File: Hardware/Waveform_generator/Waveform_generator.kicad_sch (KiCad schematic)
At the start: 101 parts, among them J1 Conn_01x02, J2 Conn_01x02, J3 Conn_01x02, J4 Conn_01x02, J5 PogoPin, J6 PogoPin, J7 GND_CHASIS, J8 GND_CHASIS, SW1 SW_DPDT_x2, U1 TPS54202DDC, U10 MCP4822, U11 LM1875, U2 TL072, U3 ESP32-DEVKITC-32U, U4 TSR1-2450E, U5 XC6206PxxxMR, U6 AD9837BCPZ-RL7, U7 TL072, U8 AD5160, U9 TL072, Y1 X1G0041710027

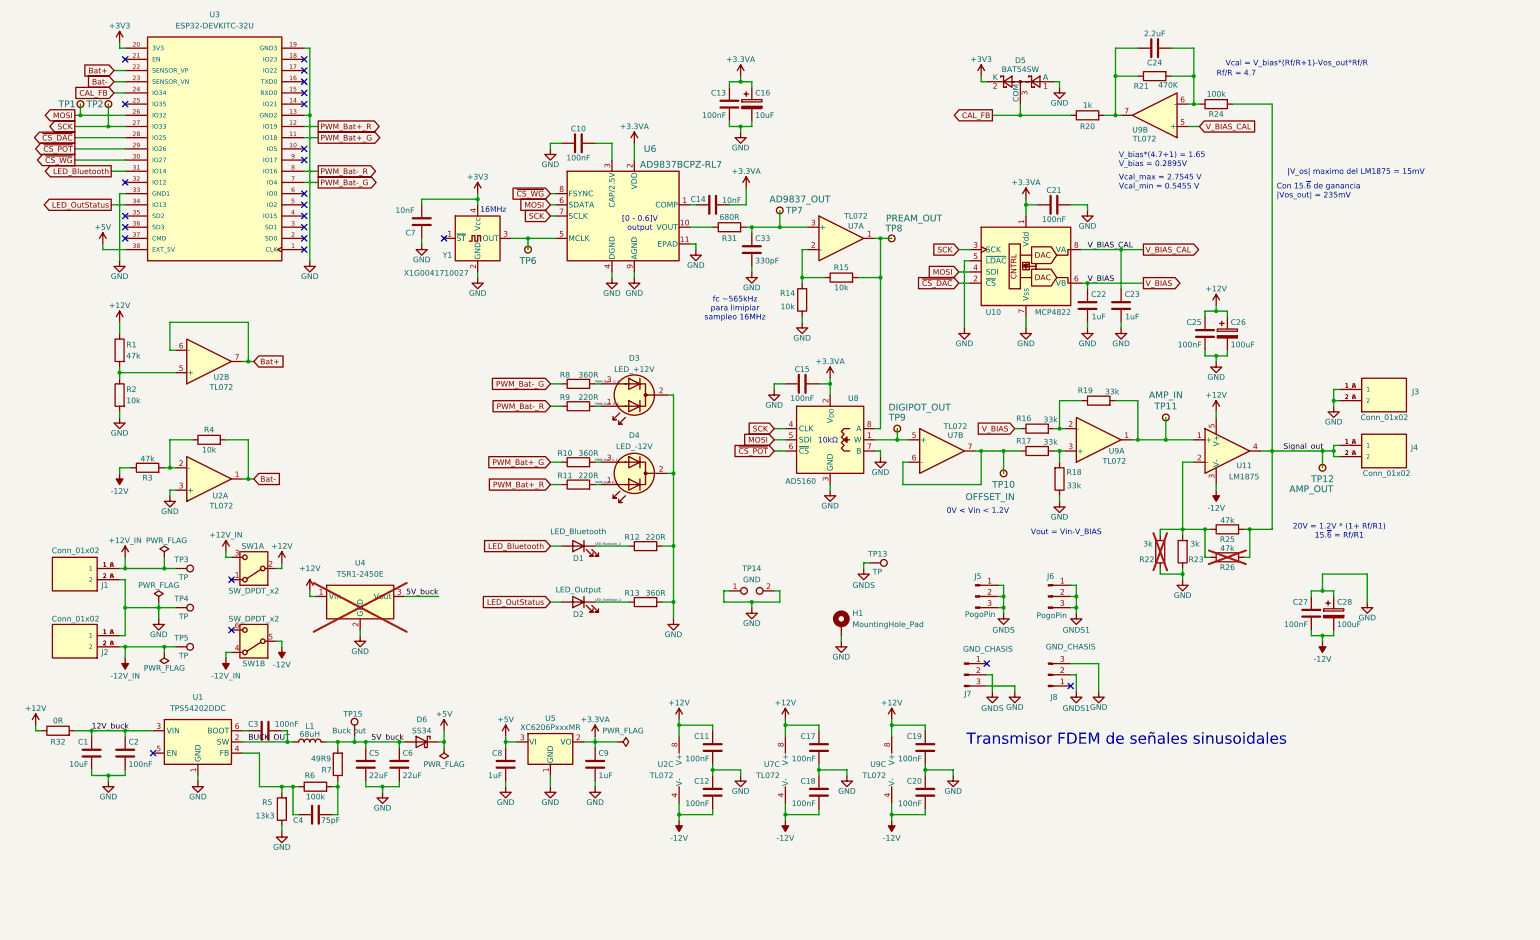
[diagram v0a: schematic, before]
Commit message: Añadido switch para el output en el esquemático
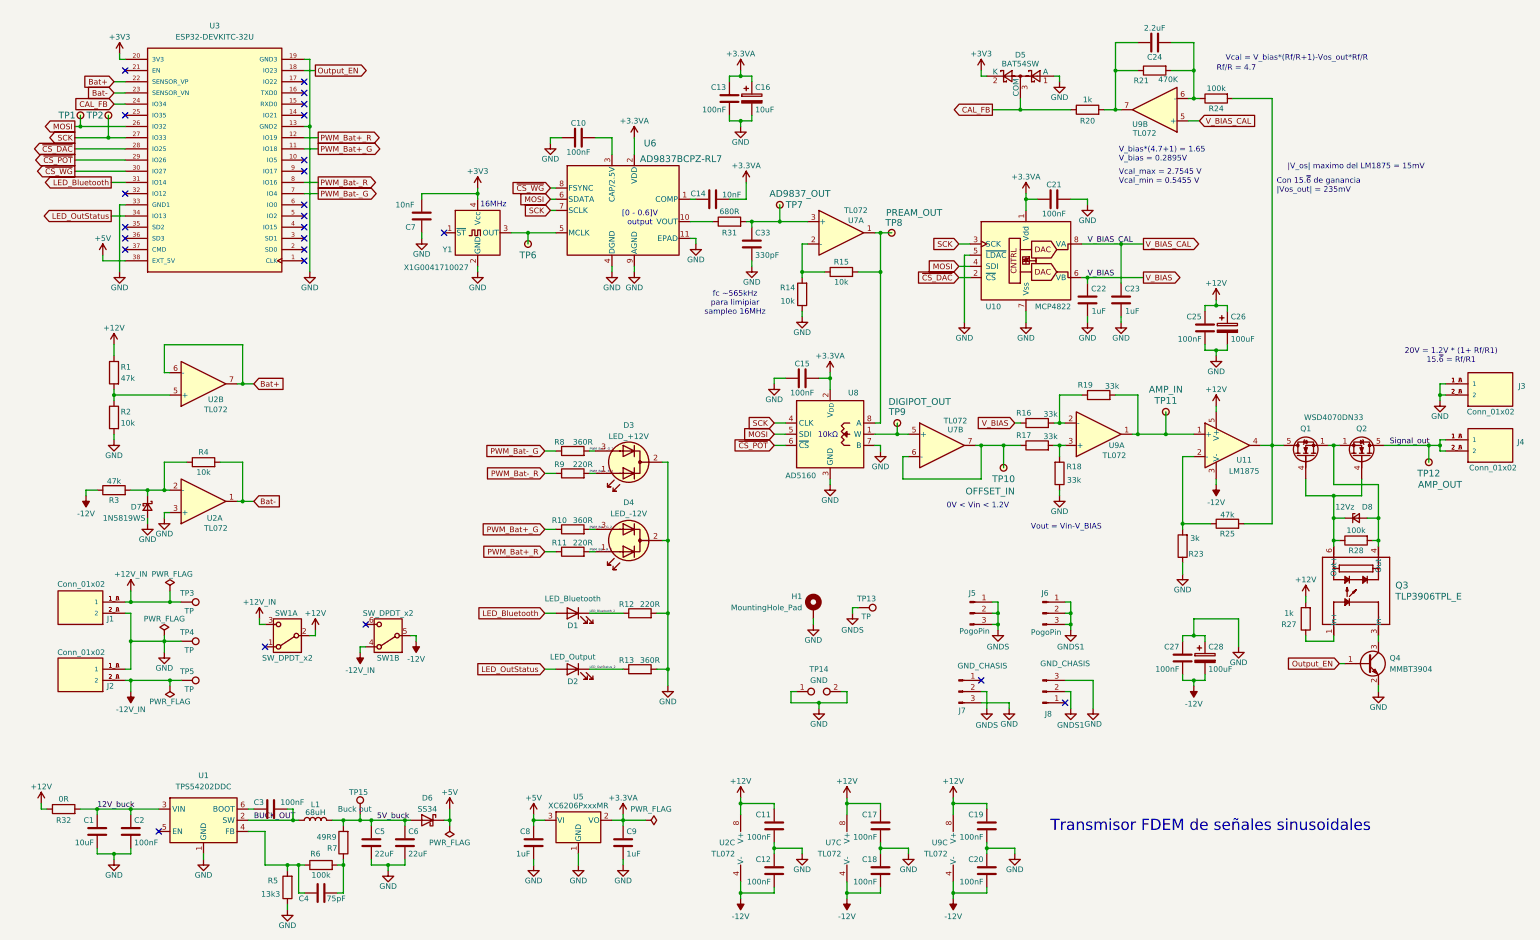
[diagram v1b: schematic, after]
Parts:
- removed R22: 3k, Resistor_THT:R_Axial_DIN0207_L6.3mm_D2.5mm_P7.62mm_Horizontal, symbol Device:R
- removed R26: 47k, Resistor_THT:R_Axial_DIN0207_L6.3mm_D2.5mm_P7.62mm_Horizontal, symbol Device:R
- removed U4: TSR1-2450E, Converter_DCDC:Converter_DCDC_TRACO_TSR1-xxxxE_THT, symbol Converter_DCDC:TSR1-2450E
- added D7: 1N5819WS, Diode_SMD:D_SOD-323_HandSoldering, symbol Device:D_Schottky_Small
- added D8: 12Vz, Diode_SMD:D_SOD-323, symbol Device:D_Zener_Small
- added Q1, Q2: WSD4070DN33, Package_SON:VSON-8_3.3x3.3mm_P0.65mm_NexFET, symbol Transistor_FET:CSD16327Q3
- added Q3: TLP3906TPL_E, 4pin SO6_TOS, symbol 2026-08-30_21-22-31:TLP3906TPL_E
- added Q4: MMBT3904, Package_TO_SOT_SMD:SOT-23, symbol Transistor_BJT:MMBT3904
- added R27: 1k, Resistor_SMD:R_0603_1608Metric_Pad0.98x0.95mm_HandSolder, symbol Device:R
- added R28: 100k, Resistor_SMD:R_0603_1608Metric_Pad0.98x0.95mm_HandSolder, symbol Device:R
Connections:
- net +12V: now also R27.2
- net GND: now also D7.2 (A), Q4.2 (E)
- net Signal_out: now also Q2.5 (D); no longer R24.2, R25.2, U11.4
- net at R3.2, R4.1, U2.2 (-): now also D7.1 (K)
- net Output_EN: now reaches U3.18 (IO23)
- net Output_EN: now also Q4.1 (B)
- new net: Q3.3 (In-), Q4.3 (C)
- new net: D8.1 (K), Q1.4 (G), Q2.4 (G), Q3.6 (Out+), R28.1
- new net: D8.2 (A), Q1.1 (S), Q1.2 (S), Q1.3 (S), Q2.1 (S), Q2.2 (S), Q2.3 (S), Q3.4 (Out-), R28.2
- new net: Q3.1 (In+), R27.1
- new net: Q1.5 (D), R24.2, R25.2, U11.4
- no-connect marks 25 -> 24
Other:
- moved on the sheet: C1, C10, C11, C12, C13, C14, C15, C16, C17, C18, C19, C2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
